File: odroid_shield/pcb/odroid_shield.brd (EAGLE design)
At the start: 83 x 48 mm, 7 parts, among them J4 ODROID_J4

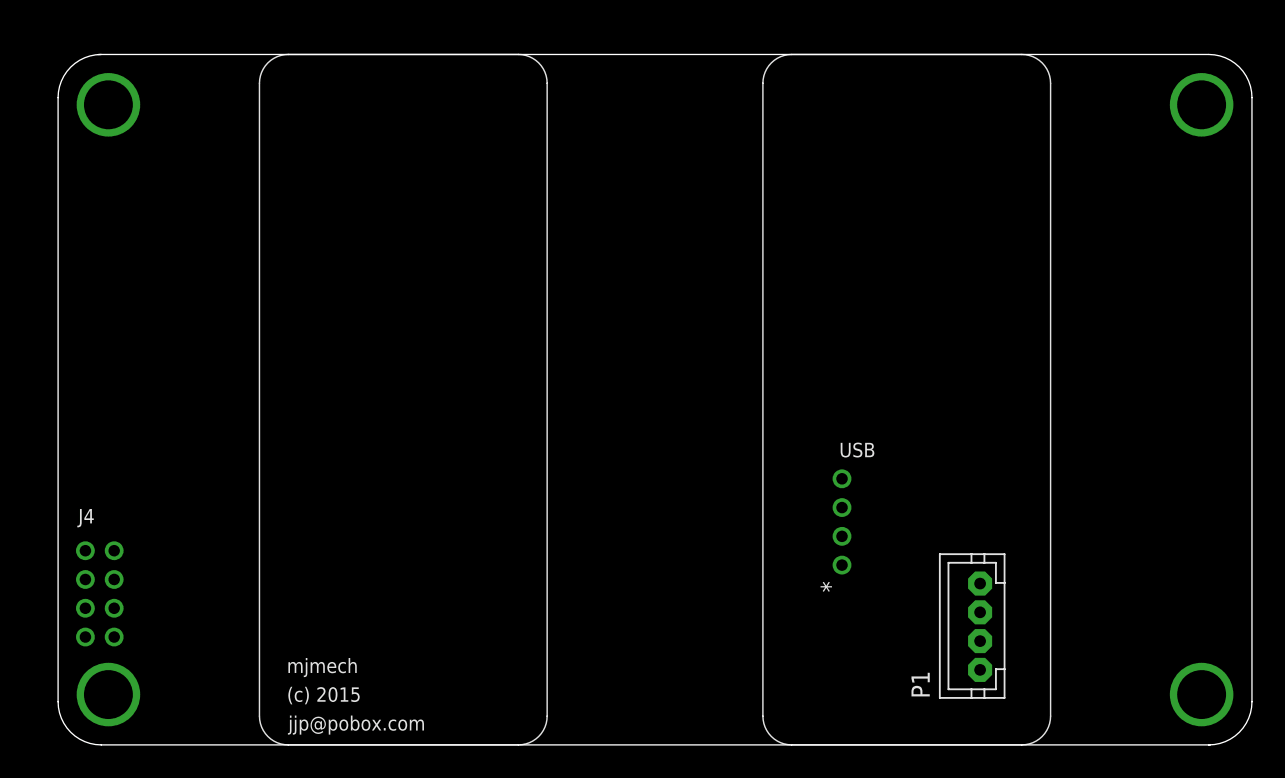
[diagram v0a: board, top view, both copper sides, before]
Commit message: Progress on odroid shield.
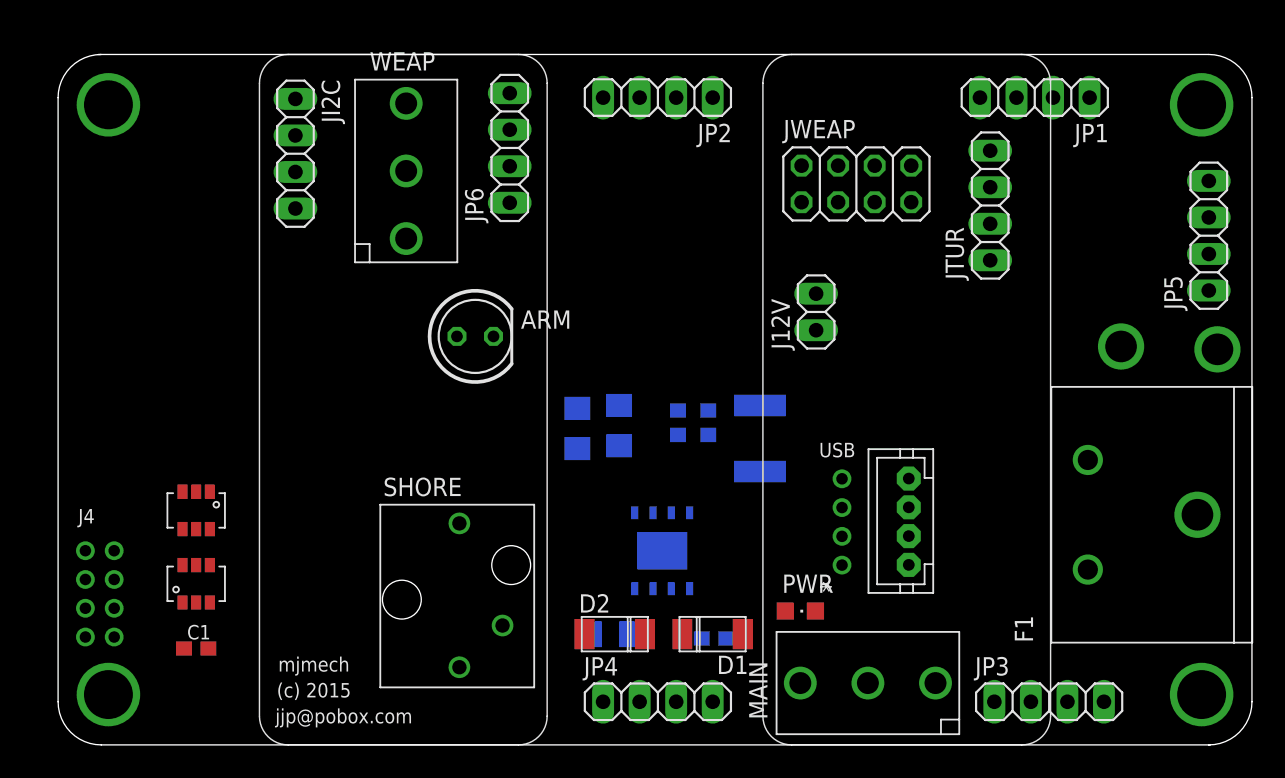
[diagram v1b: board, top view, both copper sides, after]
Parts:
- added ARM: (no value), led:LED5MM
- added B+, B-: BAT_TERM, odroid_shield:BAT_TERM
- added C1: 0.1uF, rcl:C0603
- added C2: 10uF 16V, rcl:C1206
- added C3: 1uF 16V, rcl:C0603
- added C4, C5: 22uF 16V, rcl:C1206
- added D1, D2: (no value), odroid_shield:CMS06
- added F1: FUSEMINI_0153007, odroid_shield:MINI_0153007
- added J12V: (no value), pinhead:1X02
- added JI2C, JP1, JP2, JP3, JP4, JP5, JP6, JTUR: (no value), pinhead:1X04
- added JWEAP: (no value), pinhead:2X04
- added L1: 33uH, odroid_shield:WURTH_74404042033
- added MAIN, WEAP: CK1101, odroid_shield:CK1101C
- added PWR: (no value), led:CHIPLED_0805
- added R1: 105k 1%, rcl:R0603
- added R2: 20k 1%, rcl:R0603
- added SHORE: PJ-034A, odroid_shield:PJ-034A
- added U1, U2: SINGLE-BIT_BUS_TRANSCEIVER, odroid_shield:SOT23-6
- added U3: ST1S10, odroid_shield:POWER_SO8
- moved P1 8.83 mm to (59.1, 15.5)
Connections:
- new net +5V: C4.1, C5.1, J4.8, L1.2, R1.2, U1.1, U1.5, U2.6
- new net +8V: D1.1, JP1.4, JP2.4, JP3.4, JP4.4, JP5.4, JP6.4, JTUR.4, MAIN.2
- new net GND: B-.1, C1.2, C2.2, C3.2, C4.2, C5.2, J4.7, JP1.1, JP2.1, JP3.1, JP4.1, JP5.1, JP6.1, JTUR.1, R2.1, SHORE.3, U1.2, U2.2, U3.4, U3.5, U3.8, U3.PAD
- new net N$1: P1.4, X1.VBUS
- new net N$10: L1.1, U3.7
- new net N$11: C2.1, C3.1, D1.2, D2.2, U3.1, U3.2, U3.6
- new net N$13: R1.1, R2.2, U3.3
- new net N$2: J4.4, U1.4
- new net N$3: P1.3, X1.D-
- new net N$4: J4.6, U2.3
- new net N$5: P1.2, X1.D+
- new net N$6: P1.1, X1.GND
- new net N$7: B+.1, F1.P$2
- new net N$8: F1.P$1, MAIN.1
- new net N$9: D2.1, SHORE.1
- new net ODROID_RX_5V: JP1.2, JP2.2, JP3.2, JP4.2, JP5.2, JP6.2, JTUR.2, U1.3
- new net ODROID_TX_5V: JP1.3, JP2.3, JP3.3, JP4.3, JP5.3, JP6.3, JTUR.3, U2.4
- new net VCCIO: C1.1, J4.2, U1.6, U2.1, U2.5

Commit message: Continued work on odroid shield.
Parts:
- added C10, C9: 1uF, rcl:C0603
- added C6, C7: .1uF, rcl:C0603
- added C8: 10uF 16V, rcl:C1206
- added IC1: TS5205, v-reg:SOT25
- added IND: (no value), led:CHIPLED_0805
- added J1: AVRISP6_COMPACT, odroid_shield:CON6P2R
- added R10, R7, R8, R9: 4.7k, rcl:R0603
- added R11, R6: 200, rcl:R0603
- added R3, R4: 500, rcl:R0603
- added R5: 100k, rcl:R0603
- added SER2: (no value), pinhead:1X04
- added T1: (no value), zetex:SOT-23
- added U$5: MP33926, odroid_shield:PQFN32
- added U$6: TCA9517MSOP8, odroid_shield:MSOP8
- added U4: ATMEGA644P-20AU, odroid_shield:QFP80P1200X1200X120-44N
- moved JP6 7.51 mm to (23.9, 41.2)
- moved WEAP 5.00 mm to (29.2, 39.8)
- moved JI2C 3.00 mm to (19.5, 41.1)
- moved U2 1.24 mm to (10.8, 10.9), turned to 270 degrees
- moved U1 1.14 mm to (10.7, 16.0)
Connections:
- new net +3V3: C9.1, IC1.5, JWEAP.5
- new net AEG_PWM: U$5.2, U4.13
- new net AGITATOR_PWM: U$5.1, U4.14
- new net MOTOR_D1: U$5.26, U4.21
- new net MOTOR_D2: U$5.16, U4.22
- new net MOTOR_EN: U$5.10, U4.23
- new net MOTOR_FB: R6.2, U$5.8, U4.37
- new net N$12: JWEAP.1, U$5.12, U$5.13, U$5.14, U$5.15
- new net N$14: JWEAP.3, U$5.27, U$5.28, U$5.29, U$5.30
- new net N$15: C6.1, C7.1, C8.1, R3.2, U$5.11, U$5.31, U$5.4, U$5.6, WEAP.2
- new net N$16: C6.2, U$5.32
- new net N$17: R5.1, U$5.21
- new net N$18: IND.C
- new net N$19: JWEAP.6, T1.1
- new net N$20: ARM.A, R3.1
- new net N$21: J1.5, U4.4
- new net N$22: PWR.A, R4.1
- new net N$23: J1.3, U4.3
- new net N$24: J1.4, U4.1
- new net N$25: J1.1, U4.2
- new net N$26: SER2.3, U4.12
- new net N$27: SER2.2, U4.11
- new net N$28: IND.A, R11.1
- new net N$29: R11.2, U4.24
- new net ODROID_SCL: J4.1, R7.1, U$6.2
- new net ODROID_SDA: J4.3, R8.1, U$6.3
- new net SYS_SCL: JI2C.3, R10.1, U$6.7, U4.19
- new net SYS_SDA: JI2C.2, R9.1, U$6.6, U4.20
- net +5V: now also C10.1, IC1.1, IC1.3, J1.2, JI2C.1, R10.2, R5.2, R9.2, SER2.4, U$5.3, U$6.5, U$6.8, U4.17, U4.27, U4.38, U4.5
- net +8V: now also R4.2, WEAP.1
- net GND: now also ARM.K, C10.2, C7.2, C8.2, C9.2, IC1.2, J1.6, JI2C.4, JWEAP.2, JWEAP.4, PWR.C, R6.1, SER2.1, T1.2, U$5.18, U$5.19, U$5.20, U$5.22, U$5.23, U$5.24, U$5.5, U$5.G0, U$5.G1, U$5.G10, U$5.G11, U$5.G12, U$5.G13, U$5.G14, U$5.G15, U$5.G16, U$5.G2, U$5.G3, U$5.G4, U$5.G5, U$5.G6, U$5.G7, U$5.G8, U$5.G9, U$6.4, U4.18, U4.28, U4.39, U4.6
- net ODROID_RX_5V: now also U4.10
- net ODROID_TX_5V: now also U4.9
- net VCCIO: now also R7.2, R8.2, U$6.1

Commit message: Further progress on odroid shield.
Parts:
- removed J12V: (no value), pinhead:1X02
- removed JP1, JP2, JP3, JP4, JP5, JP6, JTUR: (no value), pinhead:1X04
- added C11, C12: 20pF, rcl:C0603
- added JD1, JD2, JD3, JD4, JD5: JST-XH4SMT_RA, odroid_shield:JST_XH_SMT_RA_4
- added JD6, JD7: JST-XH4VERT, odroid_shield:JST_XH_VERT_4
- added R12: 100k, rcl:R0603
- added U$7: ABM8G, odroid_shield:ABM8G
- added U$8: MAX21000, odroid_shield:LGA16
- F1: value FUSEMINI_0153007 -> FUSE; device odroid_shield:MINI_0153007 -> odroid_shield:KEYSTONE_HORIZ_FUSE_CLIP
- SHORE: value PJ-034A -> PJ-034ASMT; device odroid_shield:PJ-034A -> odroid_shield:CUI_PJ_015AH_SMT
- moved J1 16.3 mm to (20.8, 41.1)
- moved JI2C 15.7 mm to (27.2, 27.4), turned to 180 degrees
- moved MAIN 13.4 mm to (64.8, 14.6), turned to 0 degrees
- moved C5 11.3 mm to (47.3, 20.4), flipped to the top, turned to 90 degrees
- moved ARM 9.44 mm to (20.5, 32.5)
- moved R3 7.96 mm to (26.0, 33.2), turned to 180 degrees
- moved L1 7.83 mm to (45.5, 14.2), flipped to the top
- moved R5 7.62 mm to (42.7, 36.5), turned to 0 degrees
- moved SHORE 5.94 mm to (26.6, 14.1)
- moved C4 5.91 mm to (44.6, 20.3), flipped to the top, turned to 90 degrees
- moved T1 5.82 mm to (58.3, 38.4), flipped to the bottom, turned to 270 degrees
- moved U$5 5.71 mm to (42.3, 30.6)
- moved B- 5.51 mm to (73.5, 22.2)
- moved B+ 5.46 mm to (79.3, 22.2)
- moved C7 5.09 mm to (38.7, 37.2), turned to 180 degrees
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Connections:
- new net N$32: C12.1, U$7.1, U4.7
- new net N$33: C11.1, U$7.3, U4.8
- net +3V3: now also JI2C.1, R10.2, R12.2, R9.2, U$6.5, U$6.8, U$8.1, U$8.14, U$8.15
- net +5V: no longer JI2C.1, R10.2, R9.2, U$6.5, U$6.8
- net +8V: now also JD1.4, JD2.4, JD3.4, JD4.4, JD5.4, JD6.4, JD7.4; no longer JP1.4, JP2.4, JP3.4, JP4.4, JP5.4, JP6.4, JTUR.4
- net GND: now also C11.2, C12.2, IND.C, JD1.1, JD2.1, JD3.1, JD4.1, JD5.1, JD6.1, JD7.1, U$7.2, U$7.4, U$8.5, U$8.8; no longer JP1.1, JP2.1, JP3.1, JP4.1, JP5.1, JP6.1, JTUR.1
- net N$18: now also R12.1, U$8.7; no longer IND.C
- net N$7: now also F1.3, F1.4; no longer F1.P$2
- net N$8: now also F1.1, F1.2; no longer F1.P$1
- net ODROID_RX_5V: now also JD1.2, JD2.2, JD3.2, JD4.2, JD5.2, JD6.2, JD7.2; no longer JP1.2, JP2.2, JP3.2, JP4.2, JP5.2, JP6.2, JTUR.2
- net ODROID_TX_5V: now also JD1.3, JD2.3, JD3.3, JD4.3, JD5.3, JD6.3, JD7.3; no longer JP1.3, JP2.3, JP3.3, JP4.3, JP5.3, JP6.3, JTUR.3
- net SYS_SCL: now also U$8.4
- net SYS_SDA: now also U$8.6

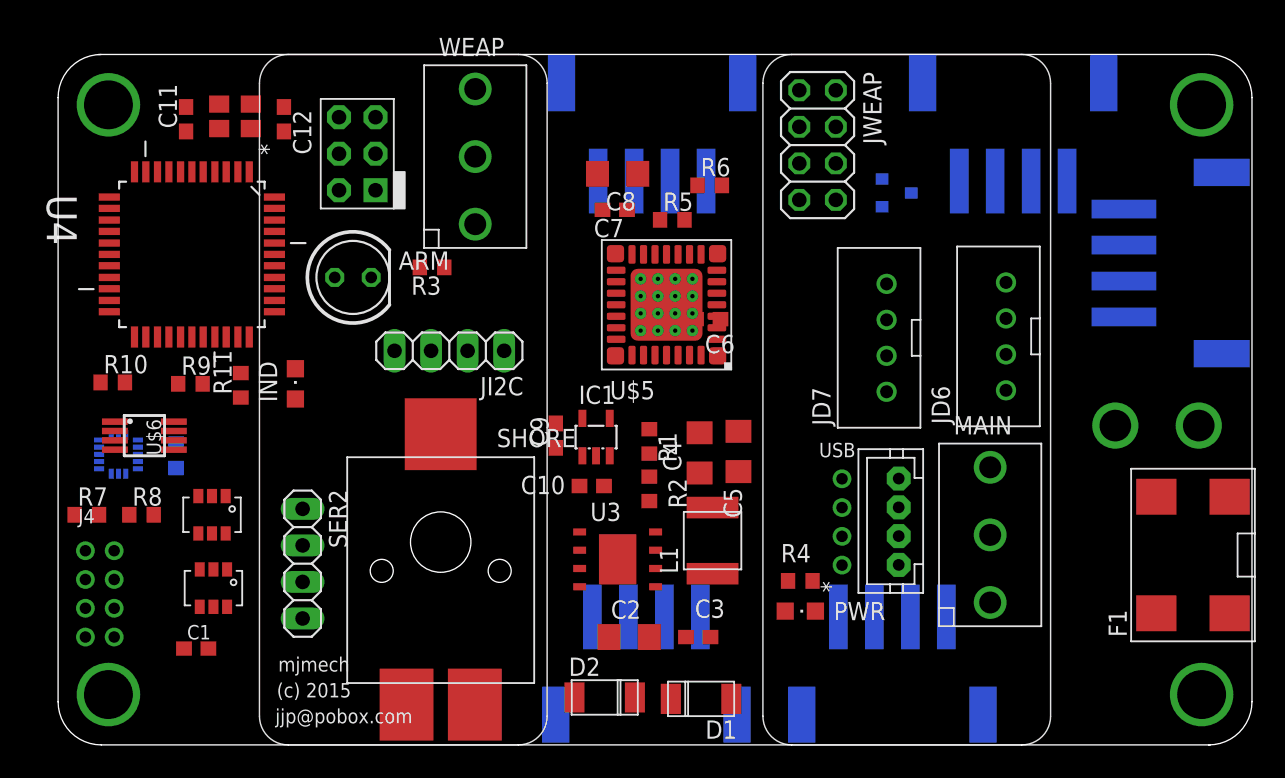
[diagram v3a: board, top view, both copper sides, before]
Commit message: odroid_shield: Complete rough draft of schematic.
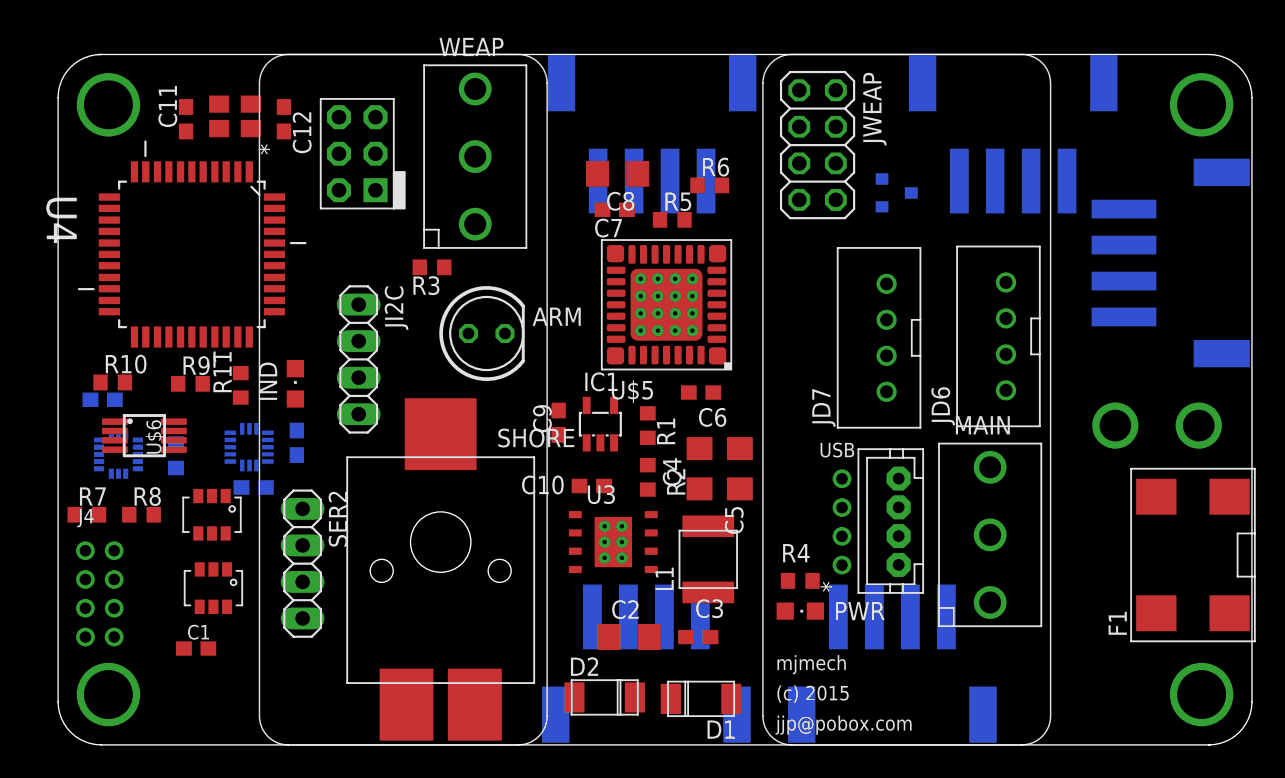
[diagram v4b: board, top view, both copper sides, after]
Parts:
- added C13, C14, C15: .1uF, rcl:C0603
- added U$9: MMA8451Q, odroid_shield:QFN16
- moved ARM 10.1 mm to (29.8, 28.6)
- moved JI2C 6.33 mm to (20.9, 26.8), turned to 270 degrees
- moved C6 5.12 mm to (44.7, 24.5)
- moved L1 1.33 mm to (45.2, 12.9)
- moved U3 1.24 mm to (38.6, 14.1)
- moved C5 1.20 mm to (47.4, 19.2)
- moved R1 1.10 mm to (41.0, 22.2)
- moved C4 1.10 mm to (44.6, 19.2)
- moved IC1 0.95 mm to (37.7, 22.3)
- moved C9 0.92 mm to (34.8, 22.4)
- moved R2 0.81 mm to (41.0, 18.6)
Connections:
- new net N$36: C15.1, U$9.2
- net +3V3: now also C13.1, C14.1, U$9.1, U$9.14, U$9.7
- net GND: now also C13.2, C14.2, C15.2, U$9.10, U$9.12, U$9.5, U3.PAD1, U3.PAD2, U3.PAD3, U3.PAD4, U3.PAD5, U3.PAD6
- net SYS_SCL: now also U$9.4
- net SYS_SDA: now also U$9.6

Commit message: odroid_shield: Fix some DPNs and move the 3.3V regulator to a slightly better spot.
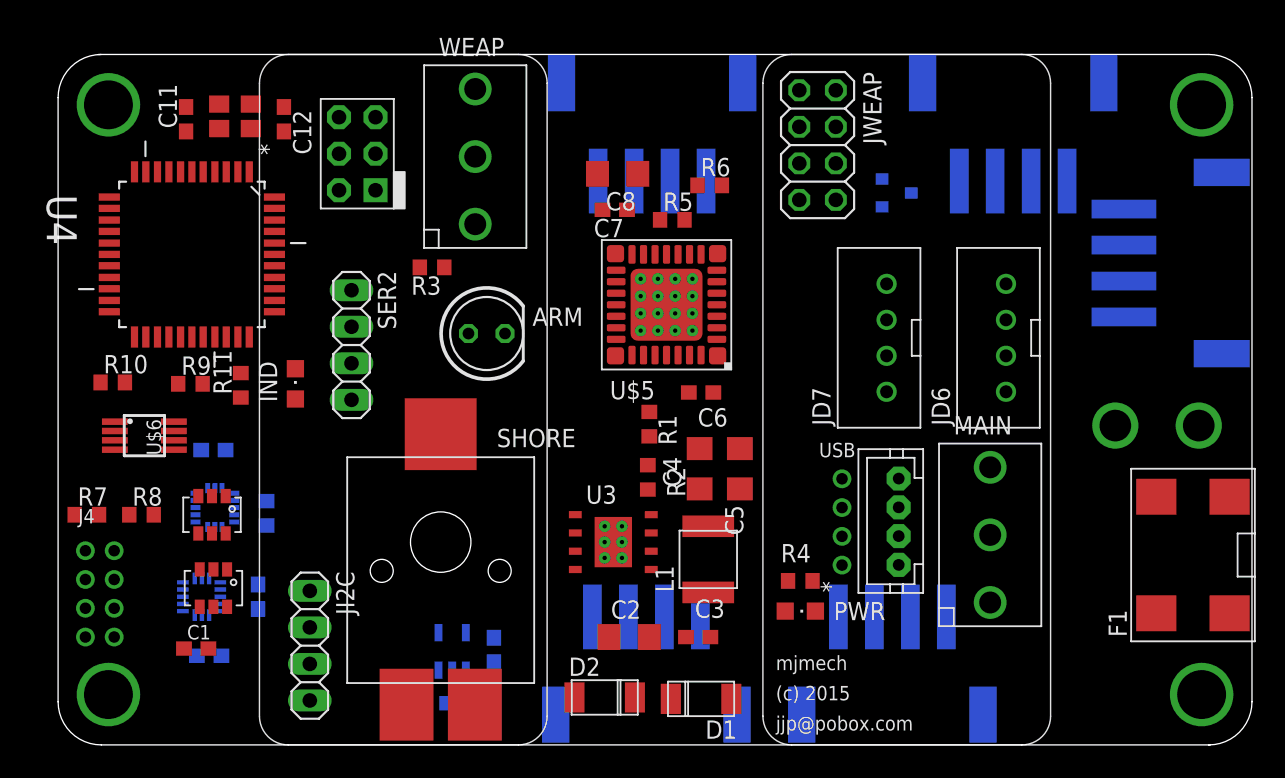
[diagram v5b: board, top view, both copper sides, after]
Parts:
- moved JI2C 20.2 mm to (17.5, 6.90)
- moved IC1 18.9 mm to (27.4, 6.50), flipped to the bottom
- moved C10 17.7 mm to (27.9, 2.90), flipped to the bottom
- moved C9 16.4 mm to (30.3, 6.60), flipped to the bottom
- moved SER2 15.6 mm to (20.4, 27.8)
- moved C14 12.1 mm to (10.5, 6.20)
- moved C15 11.0 mm to (13.9, 10.3)
- moved U$9 10.9 mm to (10.0, 10.3)
- moved C13 8.46 mm to (10.8, 20.5)
- moved U$8 7.65 mm to (10.9, 16.5)
- moved R12 7.46 mm to (14.5, 16.1)
- moved R1 0.14 mm to (41.1, 22.3)
- moved JD6 0.10 mm to (65.9, 28.3)

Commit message: odroid_shield: Tried to name all parts.  Actually connected up the laser FET.
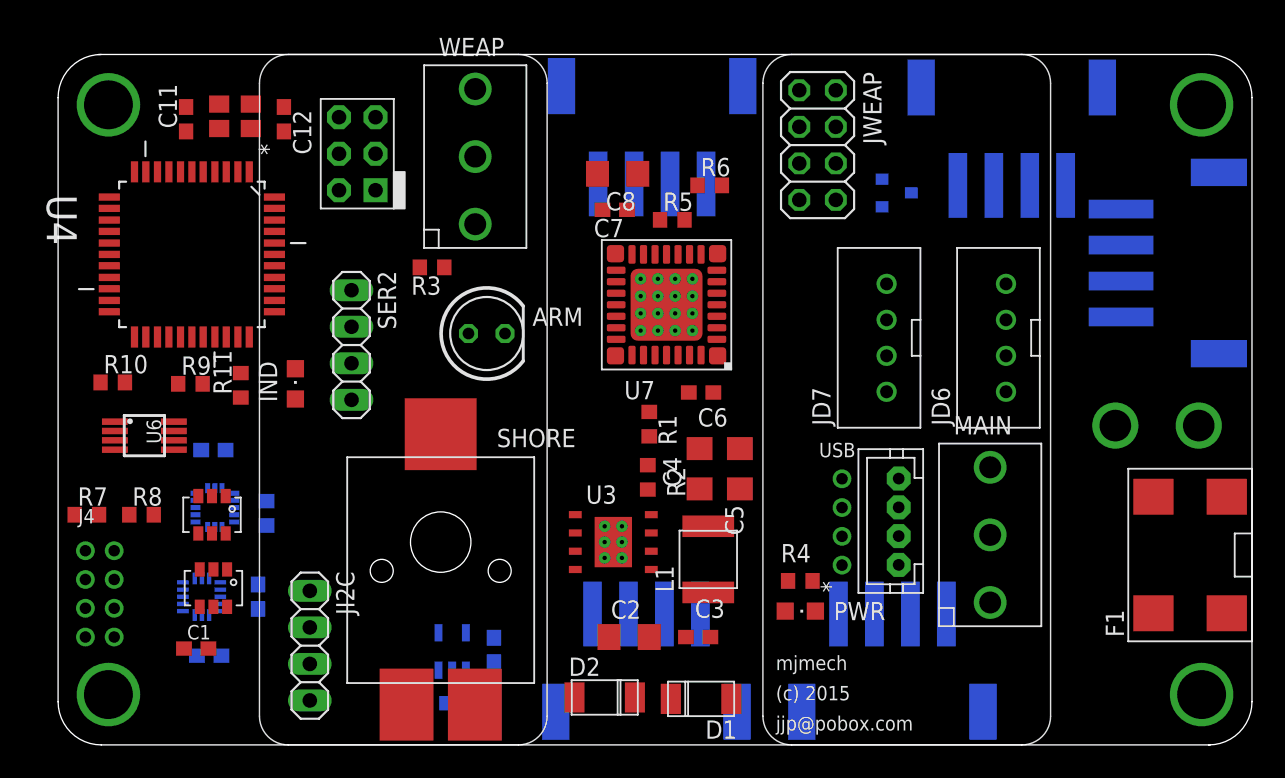
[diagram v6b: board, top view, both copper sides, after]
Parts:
- moved JD2 0.32 mm to (66.3, 43.5)
- moved F1 0.20 mm to (78.7, 13.2)
- moved JD3 0.20 mm to (78.5, 33.5)
- moved JD4 0.20 mm to (58.0, 4.50)
- moved JD5 0.20 mm to (40.9, 4.50)
- moved JD1 0.20 mm to (41.3, 43.6)
- renumbered IC1 to U5, P1 to JUSB, T1 to Q1, U$5 to U7, U$6 to U6, U$7 to U10, U$8 to U8, U$9 to U9, X1 to J2
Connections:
- new net LASER_EN: Q1.3, U4.25
